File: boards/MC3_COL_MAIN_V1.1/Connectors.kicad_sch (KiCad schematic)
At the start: 10 parts, among them J3 ENC_leaf1, J4 ENC_leaf2, J5 ENC_leaf3, J6 ENC_leaf4

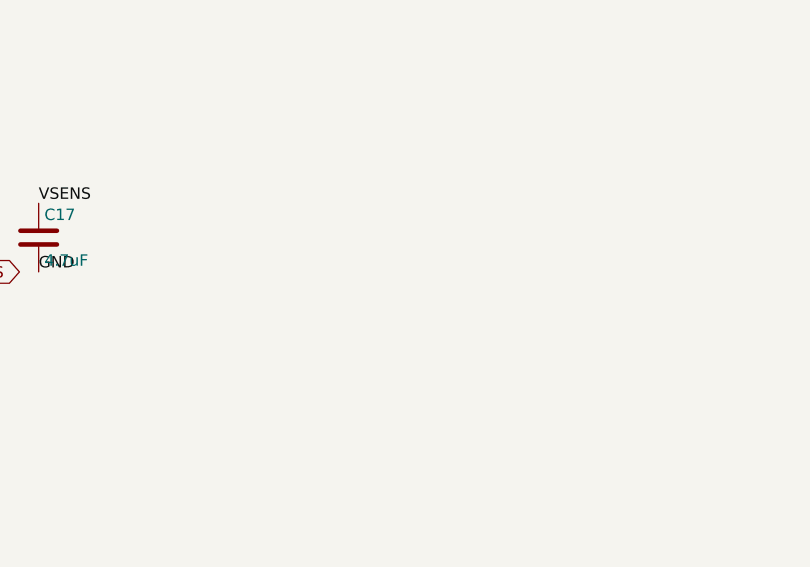
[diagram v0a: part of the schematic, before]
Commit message: V1.1: J13 machine-harness FFC (TE 84952-6, 1.0 mm 6-way) - YAW_OUT1/2 via new OUT1/OUT2 sheet pins, VIN_PAD/GND/CANH/CANL; ERC 0 errors
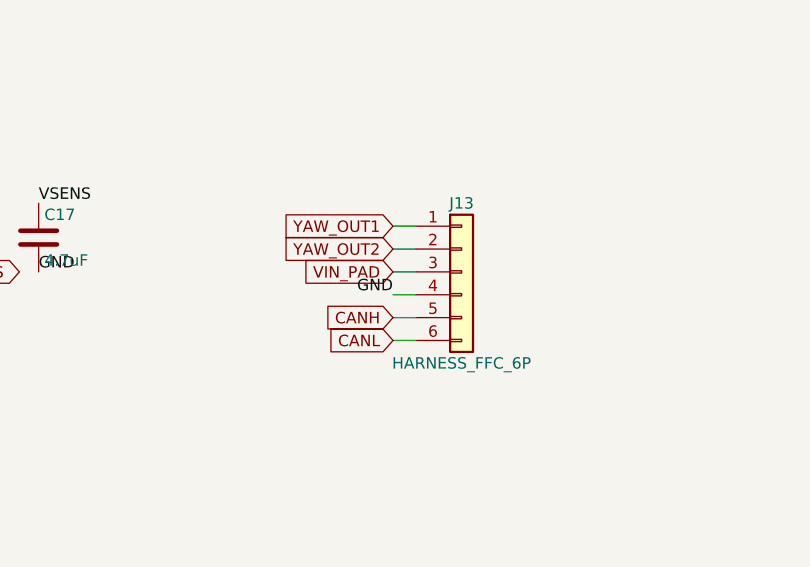
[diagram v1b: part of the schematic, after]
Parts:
- added J13: HARNESS_FFC_6P, MC3_COL_MAIN:TE_84952-6_1x06-1MP_P1.0mm_Horizontal, symbol Connector_Generic:Conn_01x06
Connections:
- net GND: now also J13.4 (Pin_4)
- new net CANH: J13.5 (Pin_5)
- new net CANL: J13.6 (Pin_6)
- new net VIN_PAD: J13.3 (Pin_3)
- new net YAW_OUT1: J13.1 (Pin_1)
- new net YAW_OUT2: J13.2 (Pin_2)

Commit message: V1.1: J13 note corrected from TE catalog (2.56 mm tall, ZIF, 0.30 mm FFC)
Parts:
- J13: Note PROVISIONAL - machine harness FFC, 1.0 mm pitch 6-way, bott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 -> PROVISIONAL - machine harness FFC: TE 84952-6, 1.0 mm pitch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
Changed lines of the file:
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@@
 			)
 		)
-		(property "Note" "PROVISIONAL - machine harness FFC, 1.0 mm pitch 6-way, bottom contact, right angle, 1.0 mm tall, underside. Pin order 1 YAW_OUT1, 2 YAW_OUT2, 3 VIN_PAD (24 V), 4 GND, 5 CANH, 6 CANL: the supply pair sits between the PWM motor pair and the CAN pair as the guard (COL-COTS-0038 harness). J1/J12 bare pads stay as the fallback / pigtail solder points. Verify TE 84952 current rating (1 A/contact class) before fab."
+		(property "Note" "PROVISIONAL - machine harness FFC: TE 84952-6, 1.0 mm pitch 6-way, ZIF slide-lock, right angle, bottom contact, 2.56 mm tall x 7.3 mm deep (catalog 1-1773440-6 p.12; KiCad's '1.0 mm height' description is wrong), underside. Takes 0.30 mm FPC/FFC with >=3.8 mm backing. Pin order 1 YAW_OUT1, 2 YAW_OUT2, 3 VIN_PAD (24 V), 4 GND, 5 CANH, 6 CANL: the supply pair sits between the PWM motor pair and the CAN pair as the guard (COL-COTS-0038). J1/J12 pads stay as the fallback. Current rating is in product spec 108-1393, not the catalog - verify (yaw pair sees 0.93 A at stall)."
 			(at 152.4 63.5 0)
 			(hide yes)

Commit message: V1.1: J13 note - ratings and sourcing
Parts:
- J13: Note PROVISIONAL - machine harness FFC: TE 84952-6, 1.0 mm pitch 6-way, ZIF slide-lock, right angle, bottom contact, 2.56 mm tall x 7.3 mm deep (catalog 1-1773440-6 p.12; KiCad's '1.0 mm height' description is wrong), underside. Takes 0.30 mm FPC/FFC with >=3.8 mm backing. Pin order 1 YAW_OUT1, 2 YAW_OUT2, 3 VIN_PAD (24 V), 4 GND, 5 CANH, 6 CANL: the supply pair sits between the PWM motor pair and the CAN pair as the guard (COL-COTS-0038). J1/J12 pads stay as the fallback. Current rating is in product spec 108-1393, not the catalog - verify (yaw pair sees 0.93 A at stall). -> PROVISIONAL - machine harness FFC: TE 84952-6, 1.0 mm pitch 6-way, ZIF slide-lock, right angle, bottom contact, 2.56 mm tall x 7.3 mm deep, underside. Rated 1 A/contact, 200 V, -40..85 C (DigiKey attrs from TE spec 108-1393); takes 0.30 mm FPC/FFC with >=3.8 mm backing. Pin order 1 YAW_OUT1, 2 YAW_OUT2, 3 VIN_PAD (24 V), 4 GND, 5 CANH, 6 CANL - supply pair between the PWM motor pair and CAN as the guard (COL-COTS-0038). J1/J12 pads stay as the fallback. Sourcing: 18-week factory lead - buy distributor stock, or swap to JLC-stocked JUSHUO AFA07-S06FCA-00 (different footprint) before layout.
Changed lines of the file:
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@@
 			)
 		)
-		(property "Note" "PROVISIONAL - machine harness FFC: TE 84952-6, 1.0 mm pitch 6-way, ZIF slide-lock, right angle, bottom contact, 2.56 mm tall x 7.3 mm deep (catalog 1-1773440-6 p.12; KiCad's '1.0 mm height' description is wrong), underside. Takes 0.30 mm FPC/FFC with >=3.8 mm backing. Pin order 1 YAW_OUT1, 2 YAW_OUT2, 3 VIN_PAD (24 V), 4 GND, 5 CANH, 6 CANL: the supply pair sits between the PWM motor pair and the CAN pair as the guard (COL-COTS-0038). J1/J12 pads stay as the fallback. Current rating is in product spec 108-1393, not the catalog - verify (yaw pair sees 0.93 A at stall)."
+		(property "Note" "PROVISIONAL - machine harness FFC: TE 84952-6, 1.0 mm pitch 6-way, ZIF slide-lock, right angle, bottom contact, 2.56 mm tall x 7.3 mm deep, underside. Rated 1 A/contact, 200 V, -40..85 C (DigiKey attrs from TE spec 108-1393); takes 0.30 mm FPC/FFC with >=3.8 mm backing. Pin order 1 YAW_OUT1, 2 YAW_OUT2, 3 VIN_PAD (24 V), 4 GND, 5 CANH, 6 CANL - supply pair between the PWM motor pair and CAN as the guard (COL-COTS-0038). J1/J12 pads stay as the fallback. Sourcing: 18-week factory lead - buy distributor stock, or swap to JLC-stocked JUSHUO AFA07-S06FCA-00 (different footprint) before layout."
 			(at 152.4 63.5 0)
 			(hide yes)

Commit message: V1.1: J13 note - sourcing
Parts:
- J13: Note PROVISIONAL - machine harness FFC: TE 84952-6, 1.0 mm pitch 6-way, ZIF slide-lock, right angle, bottom contact, 2.56 mm tall x 7.3 mm deep, underside. Rated 1 A/contact, 200 V, -40..85 C (DigiKey attrs from TE spec 108-1393); takes 0.30 mm FPC/FFC with >=3.8 mm backing. Pin order 1 YAW_OUT1, 2 YAW_OUT2, 3 VIN_PAD (24 V), 4 GND, 5 CANH, 6 CANL - supply pair between the PWM motor pair and CAN as the guard (COL-COTS-0038). J1/J12 pads stay as the fallback. Sourcing: 18-week factory lead - buy distributor stock, or swap to JLC-stocked JUSHUO AFA07-S06FCA-00 (different footprint) before layout. -> PROVISIONAL - machine harness FFC: TE 84952-6, 1.0 mm pitch 6-way, ZIF slide-lock, right angle, bottom contact, 2.56 mm tall x 7.3 mm deep, underside. Rated 1 A/contact, 200 V, -40..85 C (TE spec 108-1393 via DigiKey); takes 0.30 mm FPC/FFC with >=3.8 mm backing. Pin order 1 YAW_OUT1, 2 YAW_OUT2, 3 VIN_PAD (24 V), 4 GND, 5 CANH, 6 CANL - supply pair between the PWM motor pair and CAN as the guard (COL-COTS-0038). J1/J12 pads stay as the fallback. DigiKey A101387CT-ND, distributor stock.
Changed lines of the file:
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@@
 			)
 		)
-		(property "Note" "PROVISIONAL - machine harness FFC: TE 84952-6, 1.0 mm pitch 6-way, ZIF slide-lock, right angle, bottom contact, 2.56 mm tall x 7.3 mm deep, underside. Rated 1 A/contact, 200 V, -40..85 C (DigiKey attrs from TE spec 108-1393); takes 0.30 mm FPC/FFC with >=3.8 mm backing. Pin order 1 YAW_OUT1, 2 YAW_OUT2, 3 VIN_PAD (24 V), 4 GND, 5 CANH, 6 CANL - supply pair between the PWM motor pair and CAN as the guard (COL-COTS-0038). J1/J12 pads stay as the fallback. Sourcing: 18-week factory lead - buy distributor stock, or swap to JLC-stocked JUSHUO AFA07-S06FCA-00 (different footprint) before layout."
+		(property "Note" "PROVISIONAL - machine harness FFC: TE 84952-6, 1.0 mm pitch 6-way, ZIF slide-lock, right angle, bottom contact, 2.56 mm tall x 7.3 mm deep, underside. Rated 1 A/contact, 200 V, -40..85 C (TE spec 108-1393 via DigiKey); takes 0.30 mm FPC/FFC with >=3.8 mm backing. Pin order 1 YAW_OUT1, 2 YAW_OUT2, 3 VIN_PAD (24 V), 4 GND, 5 CANH, 6 CANL - supply pair between the PWM motor pair and CAN as the guard (COL-COTS-0038). J1/J12 pads stay as the fallback. DigiKey A101387CT-ND, distributor stock."
 			(at 152.4 63.5 0)
 			(hide yes)

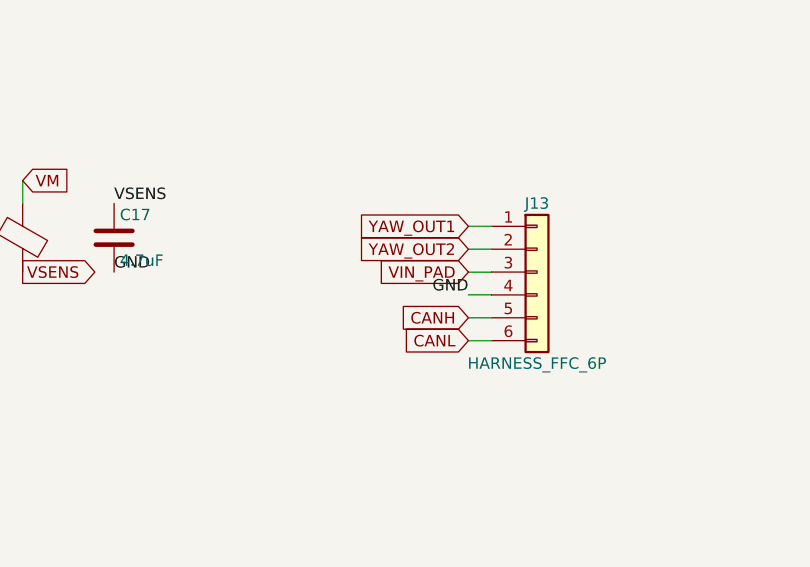
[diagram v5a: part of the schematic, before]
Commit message: V1.1: J13 pin order mirrored (CANL CANH GND VIN OUT1 OUT2) for routing
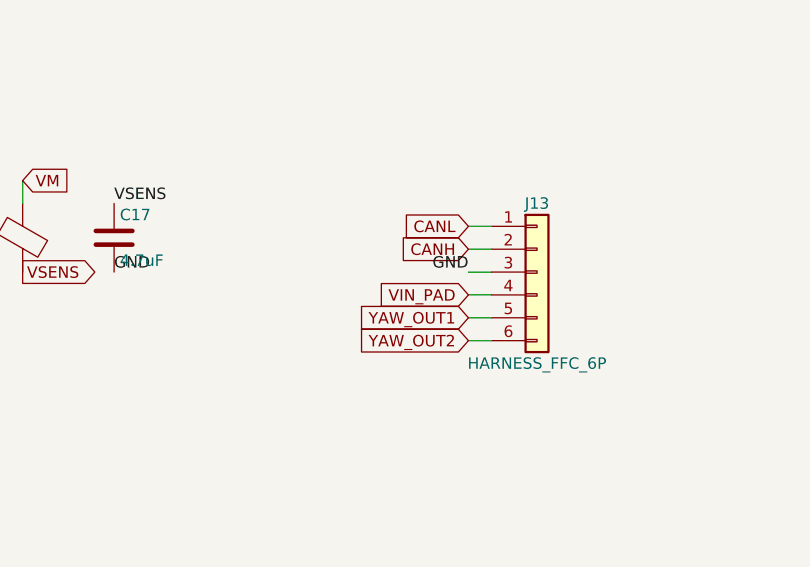
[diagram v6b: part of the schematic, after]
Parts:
- J13: Note PROVISIONAL - machine harness FFC: TE 84952-6, 1.0 mm pitch 6-way, ZIF slide-lock, right angle, bottom contact, 2.56 mm tall x 7.3 mm deep, underside. Rated 1 A/contact, 200 V, -40..85 C (TE spec 108-1393 via DigiKey); takes 0.30 mm FPC/FFC with >=3.8 mm backing. Pin order 1 YAW_OUT1, 2 YAW_OUT2, 3 VIN_PAD (24 V), 4 GND, 5 CANH, 6 CANL - supply pair between the PWM motor pair and CAN as the guard (COL-COTS-0038). J1/J12 pads stay as the fallback. DigiKey A101387CT-ND, distributor stock. -> PROVISIONAL - machine harness FFC: TE 84952-6, 1.0 mm pitch 6-way, ZIF slide-lock, right angle, bottom contact, 2.56 mm tall x 7.3 mm deep, underside. Rated 1 A/contact, 200 V, -40..85 C (TE spec 108-1393 via DigiKey); takes 0.30 mm FPC/FFC with >=3.8 mm backing. Pin order 1 CANL, 2 CANH, 3 GND, 4 VIN_PAD (24 V), 5 YAW_OUT1, 6 YAW_OUT2 - the GND/VIN pair sits between CAN and the PWM motor pair as the guard (COL-COTS-0038; mirrored 2026-08-27 for routing). J1/J12 pads stay as the fallback. DigiKey A101387CT-ND, distributor stock.
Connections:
- net CANH: now also J13.2 (Pin_2); no longer J13.5 (Pin_5)
- net CANL: now also J13.1 (Pin_1); no longer J13.6 (Pin_6)
- net GND: now also J13.3 (Pin_3); no longer J13.4 (Pin_4)
- net VIN_PAD: now also J13.4 (Pin_4); no longer J13.3 (Pin_3)
- net YAW_OUT1: now also J13.5 (Pin_5); no longer J13.1 (Pin_1)
- net YAW_OUT2: now also J13.6 (Pin_6); no longer J13.2 (Pin_2)
